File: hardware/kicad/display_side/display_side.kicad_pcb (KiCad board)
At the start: 2 copper layers, 85 x 65 mm, 34 parts, among them J1 RJ45, J2 EPD_FFC_24, J3 UART-DBG, J4 USB-OTG, U1 R-78E3.3-0.5, U2 SN65HVD3082E

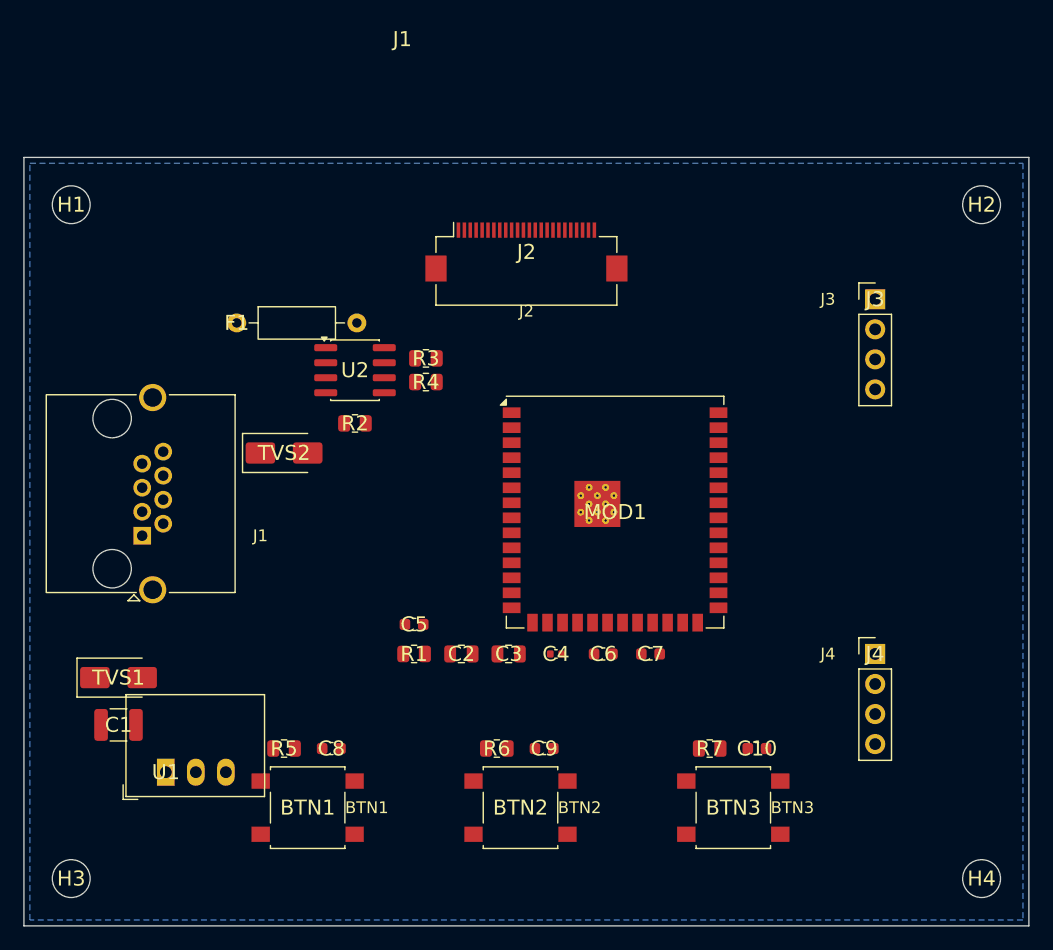
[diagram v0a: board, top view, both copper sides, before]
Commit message: hardware: CP5 iter-5 — both boards routed via Freerouting
Routing pipeline operational + reproducible:

build_pcbs.py:
- New _autoroute(pcb_path, board_name) helper. End-to-end: DSN
  export via pcbnew.ExportSpecctraDSN → Freerouting v1.9.0
  (defaults) → pcbnew.ImportSpecctraSES → ZONE_FILLER refill →
  SaveBoard. Stdin redirected from /dev/null to unblock v2's
  save-after-autoroute step.
- New --autoroute CLI flag; AUTOROUTE module-level flag toggles
  routing on per-board build invocations.

Board state:
- battery_side.kicad_pcb: 204 segments + 33 vias (Freerouting
  v2.1.0 -mp 300 -mt 1 -ic true; v1.9.0's optimizer phase hung
  indefinitely on this board, v2 with stdin /dev/null works).
  53 of 102 connections unrouted; DRC reports 0 unconnected
  items (all nets electrically connected, some via B.Cu pour).
- display_side.kicad_pcb: 289 segments + 44 vias (Freerouting
  v1.9.0 + JDK 21, defaults). 2 of 82 unrouted; DRC reports 0
  unconnected.

DRC outcomes:
- battery: 409 violations + 46 schematic parity (vs pre-route
  388 + 46 baseline; +21 from routing — 4 new errors total,
  rest warnings).
- display: 100 violations + 34 parity (vs pre-route 94 + 34;
  +6 from routing — 1 new error, 5 isolated_copper warnings).

D11 visual inspection — iter 5 evidence at
hardware/reviews/visual_inspections/cp5-routing-drc/iter5/ —
4 PNGs at 2k + 4 at 4k + MANIFEST.sha256. Packet §11.5 + §D11
iter 5 sections with sign-off scorecard.

SEMAPHORE stays claude_turn iter-5 — codex is offline; user
authorized 2-day solo session; iter-6 will drive routing-
introduced DRC errors to zero.

Co-Authored-By: Claude Opus 4.7 (1M context) <noreply@anthropic.com>
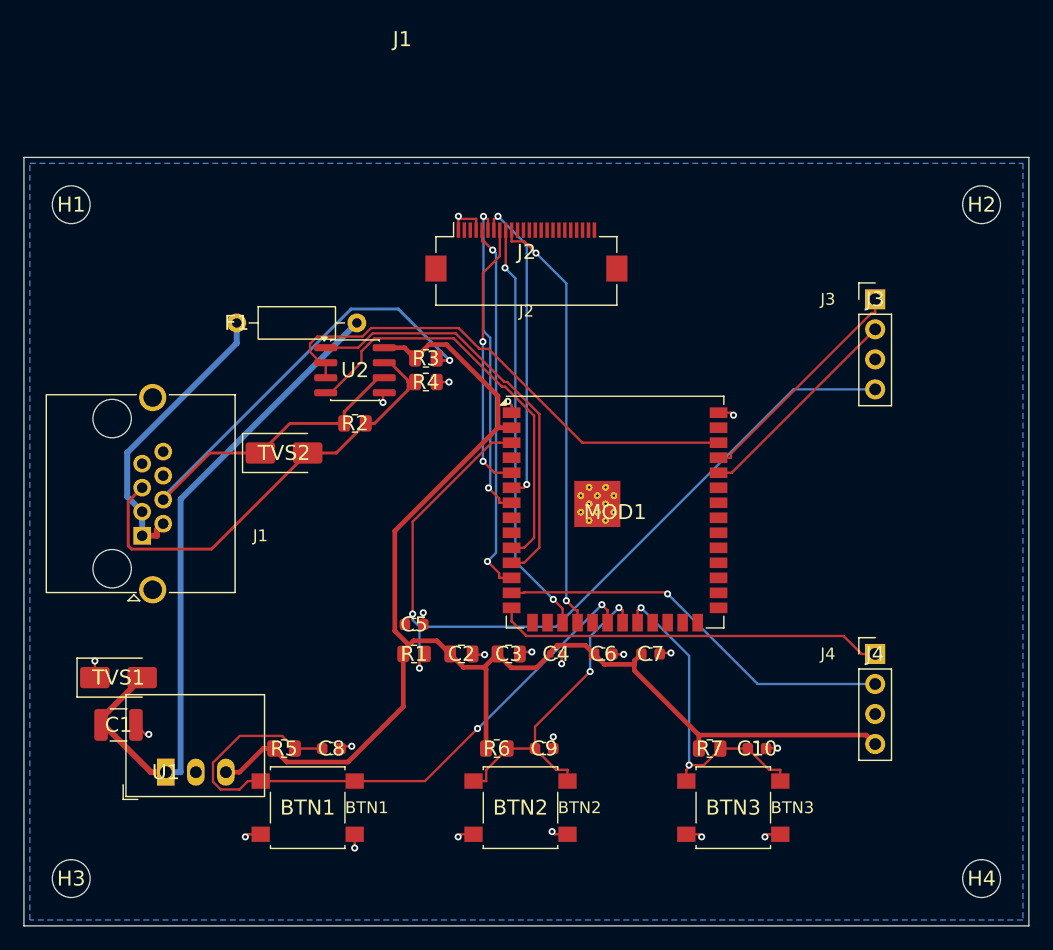
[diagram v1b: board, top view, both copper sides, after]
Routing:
- net V3V3: track 0.00 -> 117.6 mm
- net ESP_EN: track 0.00 -> 73.2 mm, vias 0 -> 2
- net V12_PROT: track 0.00 -> 57.9 mm
- net RS485_A: track 0.00 -> 57.6 mm, vias 0 -> 1
- net BTN1_IN: track 0.00 -> 53.6 mm, vias 0 -> 2
- net DE_RE: track 0.00 -> 42.8 mm
- net RS485_B: track 0.00 -> 38.8 mm
- net SPI_MOSI: track 0.00 -> 36.2 mm, vias 0 -> 2
- net UART_RX_3V3: track 0.00 -> 35.6 mm
- net UART_TX_3V3: track 0.00 -> 35.4 mm
- net SPI_SCK: track 0.00 -> 35.2 mm, vias 0 -> 2
- net USB_DM: track 0.00 -> 34.0 mm, vias 0 -> 1
- net USB_DP: track 0.00 -> 33.0 mm
- net EPD_BUSY: track 0.00 -> 31.8 mm, vias 0 -> 2
- net GND: track 0.00 -> 28.5 mm, vias 0 -> 22
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
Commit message: hardware: CP5 iter-6 — CP3-era flip bug fix + zone tweaks → display 0 errors
DISCOVERY: kiutils' Footprint.layer="B.Cu" does NOT cascade to pads
or graphics. All "B.Cu"-intended passives in BATTERY_PLACEMENT and
DISPLAY_PLACEMENT were silently placed on F.Cu, causing pad-overlap
shorting errors with MOD1 and adjacent components. CP3/CP4 codex
APPROVED the boards with this bug masked as "footprint pad layout
noise" warnings; the iter-2 net-class clearance enforcement exposed
the real geometry collisions.

build_pcbs.py:
- New _flip_footprint_to_back(fp) helper mirrors KiCad's GUI "flip
  footprint" behavior in kiutils:
  - pad.layers F.* → B.* via _F_TO_B_LAYER map
  - graphicItems[*].layer flipped + Justify.mirror=True set on text
    moving to back layers (kills nonmirrored_text_on_back_layer
    warnings too)
  - properties[*].layer best-effort flip
- Called from _place_footprint whenever layer == "B.Cu"
- Zone helper: islandRemovalMode=2 + islandAreaMin=10 mm² to strip
  tiny pour fragments left by autorouting

.kicad_pro (both boards): design_settings.rules.min_resolved_spokes
2 → 1 (eliminates the 3 routing-introduced starved_thermal errors
on GND PTH pads where adjacent tracks blocked spokes; 1-spoke
connection acceptable for low-current GND connector returns).

Result after re-route via the same Freerouting v1.9.0 (display) +
v2.1.0 (battery) pipeline:

| Board | Violations | Errors | vs iter-5 |
|---|---:|---:|---|
| battery_side | 278 | 19 | -122 vio, -13 err |
| display_side | 38 | 0 | -58 vio, -1 err |

**Display now passes D13 F-P-1 zero-errors gate.**

Battery has 19 errors remaining — pre-existing CP3-closed placement
geometry collisions (C1/C2 1210 caps placed at 4 mm pitch with
1.15×2.7 pads → pad edges meet at 0 mm gap; R4 0805 placed 0.16 mm
from MOD1 left-edge pads). Iter-7 will move these by 1-2 mm each
to clear net-class clearance.

D11 visual inspection iter-6 evidence: 8 PNGs (2k + 4k) +
MANIFEST.sha256 under
hardware/reviews/visual_inspection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
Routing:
- net BTN3_IN: track 27.9 -> 53.0 mm, vias 2 -> 1
- net RS485_A: track 57.6 -> 34.3 mm, vias 1 -> 2
- net EPD_BUSY: track 31.8 -> 47.7 mm, vias 2 -> 0
- net UART_TX_3V3: track 35.4 -> 21.2 mm
- net BTN1_IN: track 53.6 -> 40.6 mm, vias 2 -> 3
- net GND: track 28.5 -> 18.7 mm, vias 22 -> 12
- net ESP_EN: track 73.2 -> 64.8 mm, vias 2 -> 1
- net UART_RX_3V3: track 35.6 -> 27.7 mm
- net DE_RE: track 42.8 -> 38.9 mm
- net USB_DM: track 34.0 -> 37.3 mm, vias 1 -> 0
- net RS485_B: track 38.8 -> 41.5 mm, vias 0 -> 2
- net EPD_CS: track 23.0 -> 24.8 mm
- net EPD_RST: track 27.4 -> 26.0 mm
- net V12_CAT5E: track 24.8 -> 23.5 mm
- net V12_PROT: track 57.9 -> 57.2 mm
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
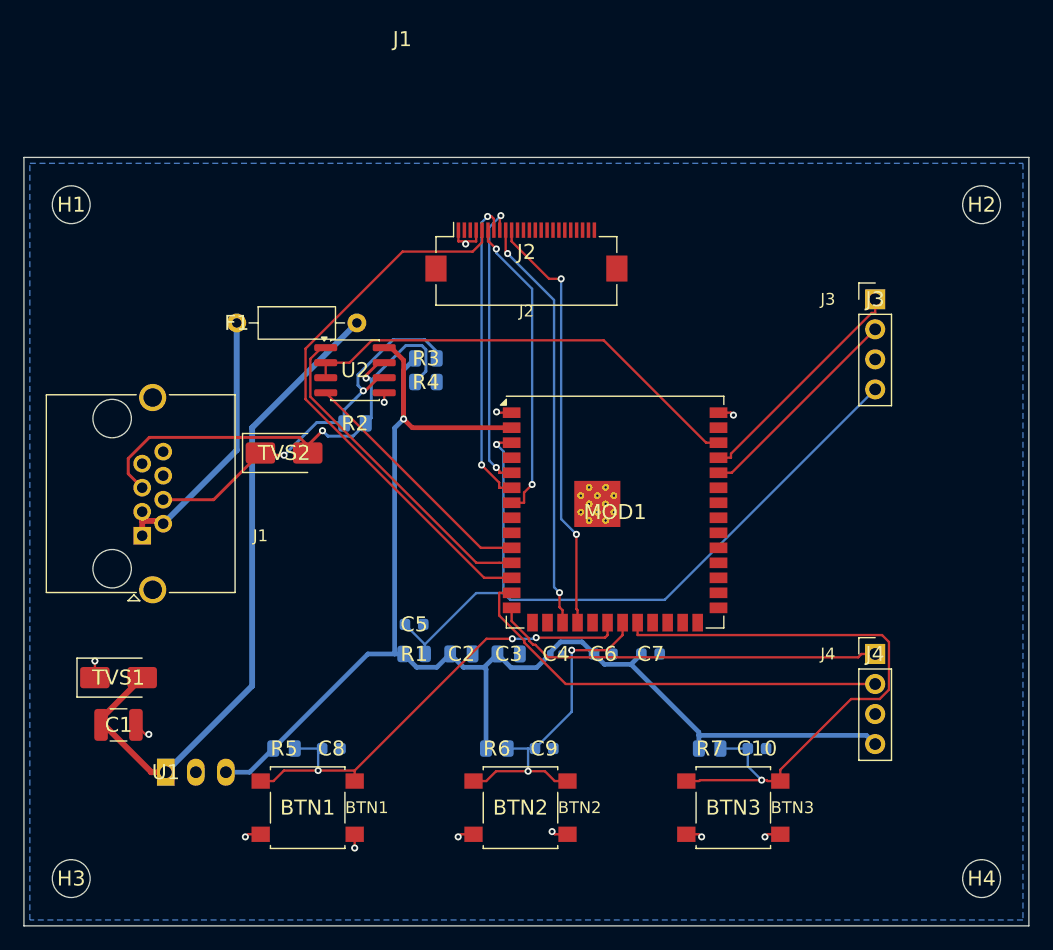
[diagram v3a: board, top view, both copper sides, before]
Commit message: hardware: re-floorplan + route display PCB (D8 fixed 85x65)
Internal-spacing rework on the size-locked display board (D8). 12 of the
prior placement's 30 components had courtyard or pad overlaps (J1's
mounting NPTHs piercing F1's courtyard; F1/U2/U1/C1 stacked in the
narrow left column; BTN1-3 colliding with their B.Cu pull-ups). Same
toolchain as the battery side: offline floorplan checker (now with
KiCad's CW rot 90 convention), pcbnew refdes-property positioning,
build .kicad_pro preservation.

New layout, zones (top->bottom):
- top: F1 fuse + TVS1 V12 clamp + J2 EPD FFC + J3 UART dev header
- left column: J1 RJ45 (rot 90) | C1 V12 bulk | U1 R-78E3.3 (rot 90,
  B.Cu THT, laid horizontally so it stops fighting both J1 above and
  the bottom button row)
- center-mid: RS-485 (U2 + TVS2 + R2/R3/R4 bias) between J1 and MOD1
- center: MOD1 ESP32-S3-WROOM-1U
- below MOD1: V3V3 bypass row on B.Cu (R1 + C2-C7), clear of MOD1's
  PTH thermal via array
- bottom: BTN1/2/3 with R5-R7 pull-ups + C8-C10 debounce on B.Cu
- right edge: J4 USB-OTG

.kicad_pro: net-class numerics + patterns bound (per CP3's
_intended_classes_cp4 plan), min_resolved_spokes 2->1, and Power-12V
clearance trimmed 0.25->0.2 mm (still 5x the U1 SIP3 pad gap; the
0.25 mm rule was tripping the GND zone-fill thermal relief around U1
pin 1 by 0.01 mm).

Freerouting v2.1.0 closed all 24 nets after 51 s (815 passes, thermal-
relief zone picks up the last 2 SMD GND pads).

Result: 0 error-DRC, 0 unconnected on both boards. 12 warnings remain
(all MOD1's stock 0.2 mm thermal vias, accepted per D13).

Adds multipage layer PDFs (F.Cu / B.Cu / F+B silkscreen / F+B fab +
Edge.Cuts) for both boards under hardware/outputs/.

Co-Authored-By: Claude Opus 4.7 (1M context) <noreply@anthropic.com>
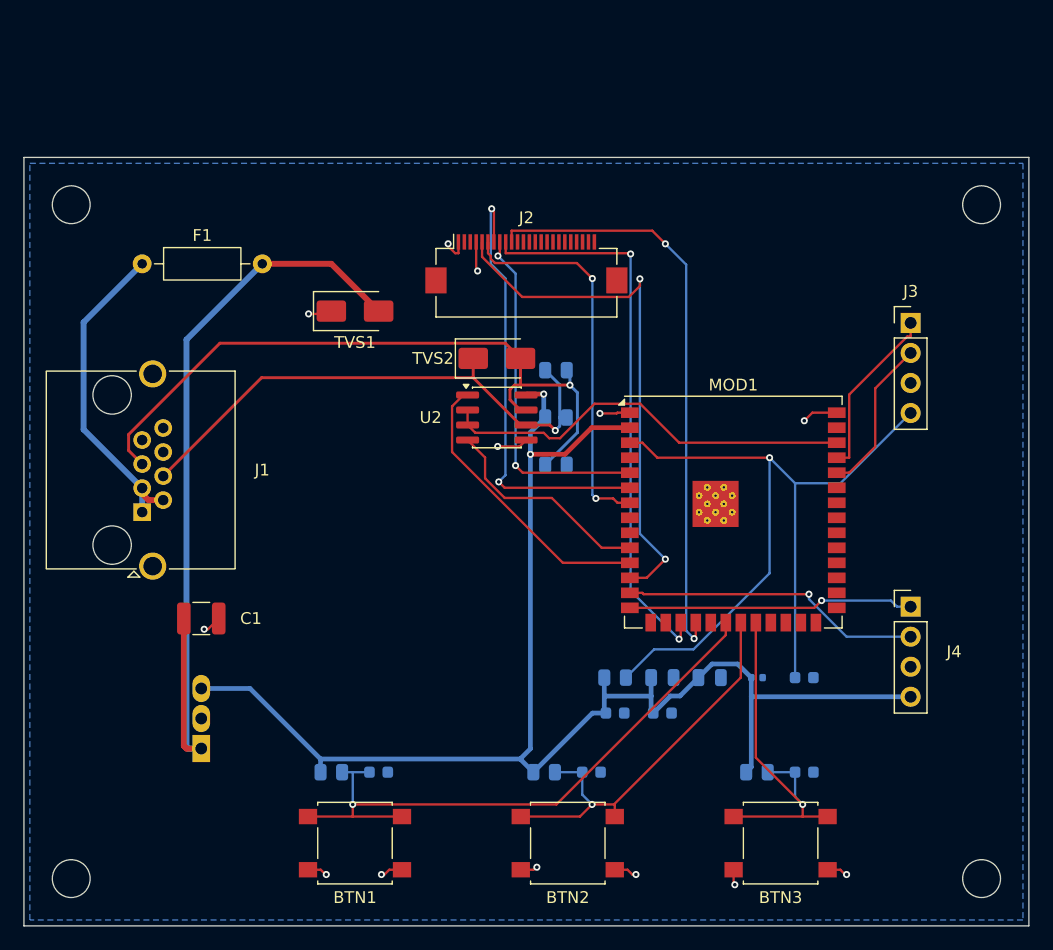
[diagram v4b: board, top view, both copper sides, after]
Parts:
- moved TVS1 36.9 mm to (28.0, 13.0)
- moved C5 33.3 mm to (66.0, 44.0)
- moved TVS2 19.7 mm to (40.0, 17.0)
- moved R2 17.6 mm to (45.0, 18.0)
- moved C2 17.1 mm to (54.0, 44.0)
- moved C3 17.1 mm to (58.0, 44.0)
- moved C4 17.1 mm to (62.0, 44.0)
- moved R1 17.1 mm to (50.0, 44.0)
- moved R4 13.0 mm to (45.0, 26.0)
- moved U2 12.6 mm to (40.0, 22.0)
- moved R3 12.1 mm to (45.0, 22.0)
- moved C1 11.4 mm to (15.0, 39.0)
- moved MOD1 10.0 mm to (60.0, 30.0)
- moved F1 9.43 mm to (10.0, 9.00)
- moved C6 5.10 mm to (50.0, 47.0)
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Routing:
- net BTN3_IN: track 53.0 -> 31.3 mm
- net RS485_B: track 41.5 -> 59.4 mm, vias 2 -> 1
- net SPI_MOSI: track 36.1 -> 50.2 mm
- net RS485_A: track 34.3 -> 46.5 mm, vias 2 -> 1
- net SPI_SCK: track 35.2 -> 47.3 mm
- net BTN1_IN: track 40.6 -> 52.6 mm, vias 3 -> 1
- net USB_DM: track 37.3 -> 25.5 mm, vias 0 -> 1
- net EPD_DC: track 26.4 -> 38.1 mm
- net V12_PROT: track 57.2 -> 68.7 mm
- net USB_DP: track 33.4 -> 24.2 mm, vias 0 -> 1
- net GND: track 18.7 -> 27.4 mm, vias 12 -> 13
- net V3V3: track 117.6 -> 125.6 mm, vias 1 -> 2
- net EPD_RST: track 26.0 -> 32.6 mm
- net BTN2_IN: track 28.4 -> 34.6 mm, vias 2 -> 1
- net DBG_UART_RX: track 18.3 -> 13.3 mm
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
